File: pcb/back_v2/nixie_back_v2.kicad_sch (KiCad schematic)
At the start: 1 part

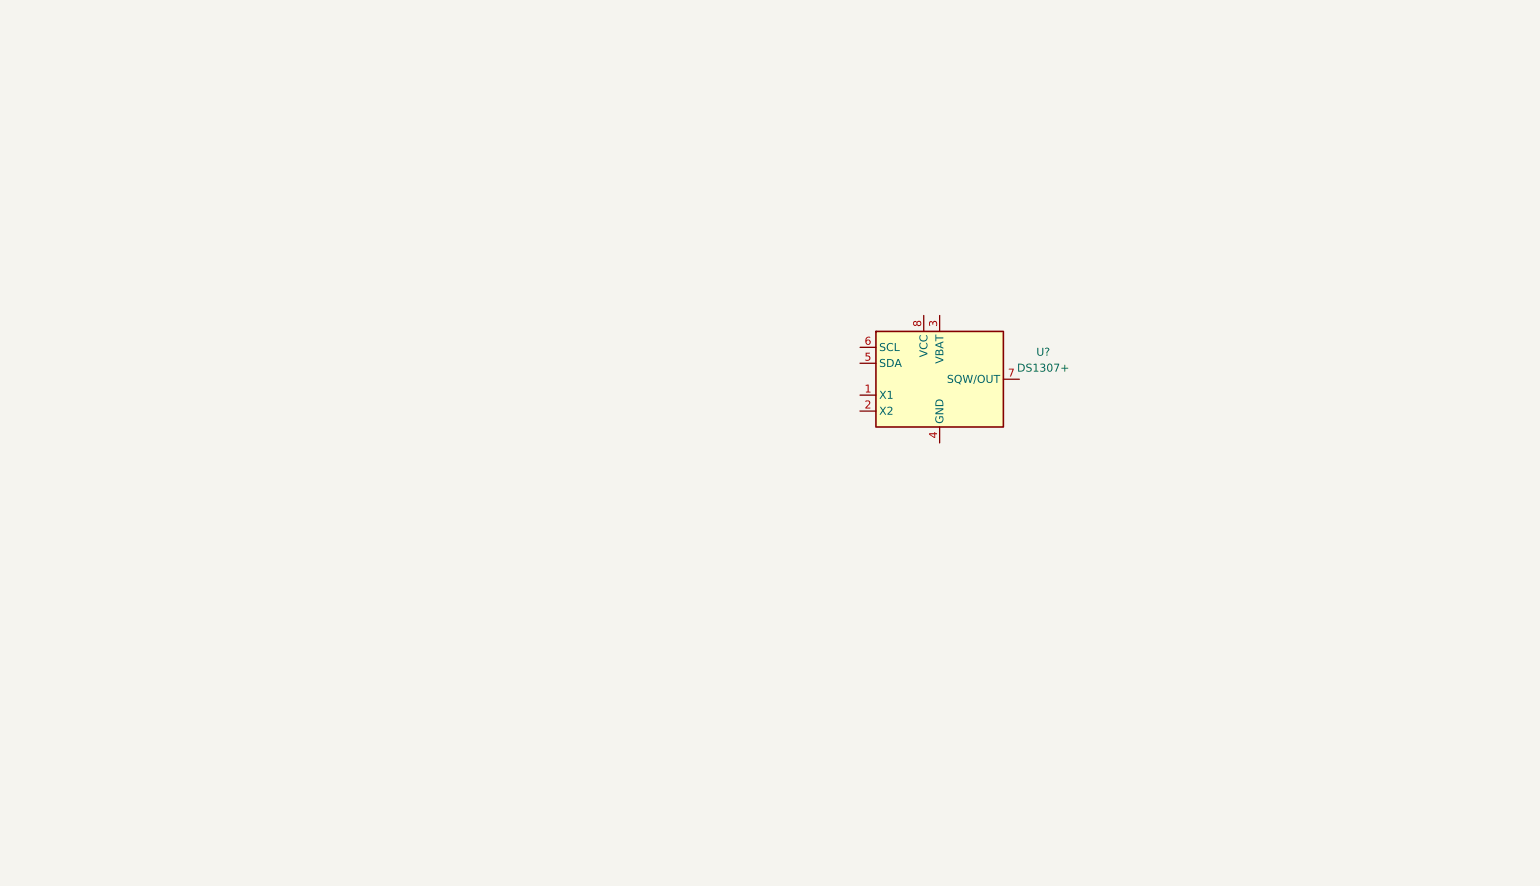
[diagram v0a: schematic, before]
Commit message: Schematic for back PCB v2
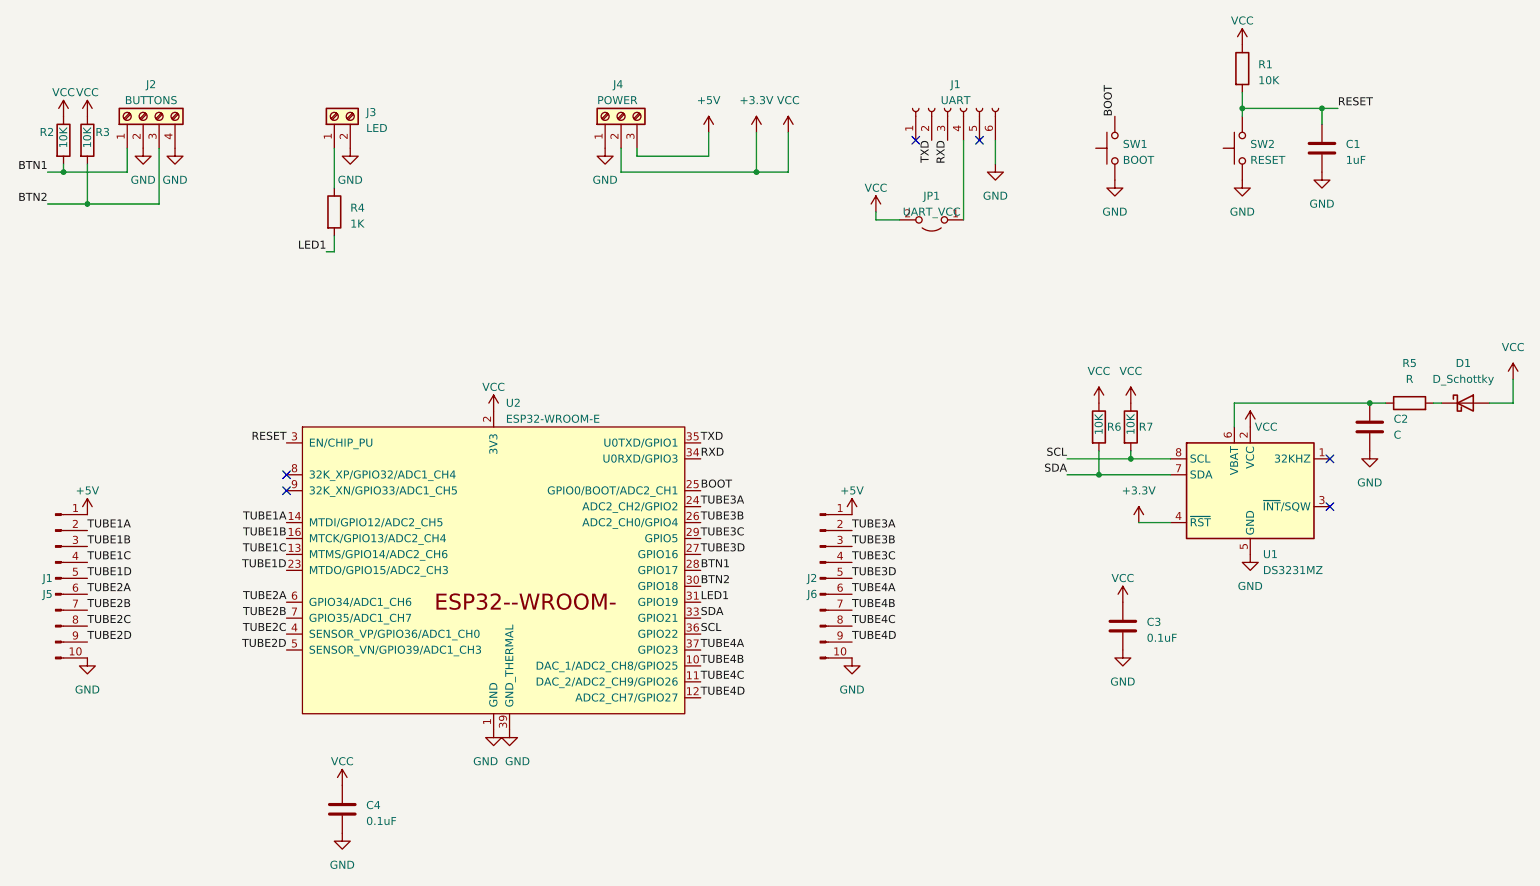
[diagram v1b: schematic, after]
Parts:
- removed U?: DS1307+, Package_DIP:DIP-8_W7.62mm, symbol Timer_RTC:DS1307+
- added C1: 1uF, symbol Device:C
- added C2: C, symbol Device:C
- added C3, C4: 0.1uF, symbol Device:C
- added D1: D_Schottky, symbol Device:D_Schottky
- added J1: UART, symbol Connector:Conn_01x06_Socket
- added J2: BUTTONS, symbol Connector:Screw_Terminal_01x04
- added J3: LED, symbol Connector:Screw_Terminal_01x02
- added J4: POWER, symbol Connector:Screw_Terminal_01x03
- added J5: J1, symbol Connector:Conn_01x10_Pin
- added J6: J2, symbol Connector:Conn_01x10_Pin
- added JP1: UART_VCC, symbol Jumper:Jumper_2_Open
- added R1, R2, R3, R6, R7: 10K, symbol Device:R
- added R4: 1K, symbol Device:R
- added R5: R, symbol Device:R
- added SW1: BOOT, symbol Switch:SW_Push
- added SW2: RESET, symbol Switch:SW_Push
- added U1: DS3231MZ, Package_SO:SOIC-8_3.9x4.9mm_P1.27mm, symbol Timer_RTC:DS3231MZ
- added U2: ESP32-WROOM-E, Espressif:ESP32-WROOM-32E, symbol Espressif:ESP32-WROOM-E
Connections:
- new net: J3.1 (Pin_1), R4.1
- new net: D1.1 (K), R5.2
- new net: J1.4 (Pin_4), JP1.1 (A)
- new net: C2.2, R5.1, U1.6 (VBAT)
- new net +3.3V: C3.1, C4.1, D1.2 (A), J4.2 (Pin_2), JP1.2 (B), R1.1, R2.1, R3.1, R6.1, R7.1, U1.2 (VCC), U1.4 (~{RST}), U2.2 (3V3)
- new net +5V: J4.3 (Pin_3), J5.1 (Pin_1), J6.1 (Pin_1)
- new net BOOT: SW1.2, U2.25 (GPIO0/BOOT/ADC2_CH1)
- new net BTN1: J2.1 (Pin_1), R2.2, U2.28 (GPIO17)
- new net BTN2: J2.3 (Pin_3), R3.2, U2.30 (GPIO18)
- new net GND: C1.2, C2.1, C3.2, C4.2, J1.6 (Pin_6), J2.2 (Pin_2), J2.4 (Pin_4), J3.2 (Pin_2), J4.1 (Pin_1), J5.10 (Pin_10), J6.10 (Pin_10), SW1.1, SW2.1, U1.5 (GND), U2.1 (GND), U2.15 (GND), U2.38 (GND), U2.39 (GND_THERMAL)
- new net LED1: R4.2, U2.31 (GPIO19)
- new net RESET: C1.1, R1.2, SW2.2, U2.3 (EN/CHIP_PU)
- new net RXD: J1.3 (Pin_3), U2.34 (U0RXD/GPIO3)
- new net SCL: R7.2, U1.8 (SCL), U2.36 (GPIO22)
- new net SDA: R6.2, U1.7 (SDA), U2.33 (GPIO21)
- new net TUBE1A: J5.2 (Pin_2), U2.14 (MTDI/GPIO12/ADC2_CH5)
- new net TUBE1B: J5.3 (Pin_3), U2.16 (MTCK/GPIO13/ADC2_CH4)
- new net TUBE1C: J5.4 (Pin_4), U2.13 (MTMS/GPIO14/ADC2_CH6)
- new net TUBE1D: J5.5 (Pin_5), U2.23 (MTDO/GPIO15/ADC2_CH3)
- new net TUBE2A: J5.6 (Pin_6), U2.6 (GPIO34/ADC1_CH6)
- new net TUBE2B: J5.7 (Pin_7), U2.7 (GPIO35/ADC1_CH7)
- new net TUBE2C: J5.8 (Pin_8), U2.4 (SENSOR_VP/GPIO36/ADC1_CH0)
- new net TUBE2D: J5.9 (Pin_9), U2.5 (SENSOR_VN/GPIO39/ADC1_CH3)
- new net TUBE3A: J6.2 (Pin_2), U2.24 (ADC2_CH2/GPIO2)
- new net TUBE3B: J6.3 (Pin_3), U2.26 (ADC2_CH0/GPIO4)
- new net TUBE3C: J6.4 (Pin_4), U2.29 (GPIO5)
- new net TUBE3D: J6.5 (Pin_5), U2.27 (GPIO16)
- new net TUBE4A: J6.6 (Pin_6), U2.37 (GPIO23)
- new net TUBE4B: J6.7 (Pin_7), U2.10 (DAC_1/ADC2_CH8/GPIO25)
- new net TUBE4C: J6.8 (Pin_8), U2.11 (DAC_2/ADC2_CH9/GPIO26)
- new net TUBE4D: J6.9 (Pin_9), U2.12 (ADC2_CH7/GPIO27)
- new net TXD: J1.2 (Pin_2), U2.35 (U0TXD/GPIO1)
- no-connect marks 0 -> 6

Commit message: Lay out the new back panel pcb
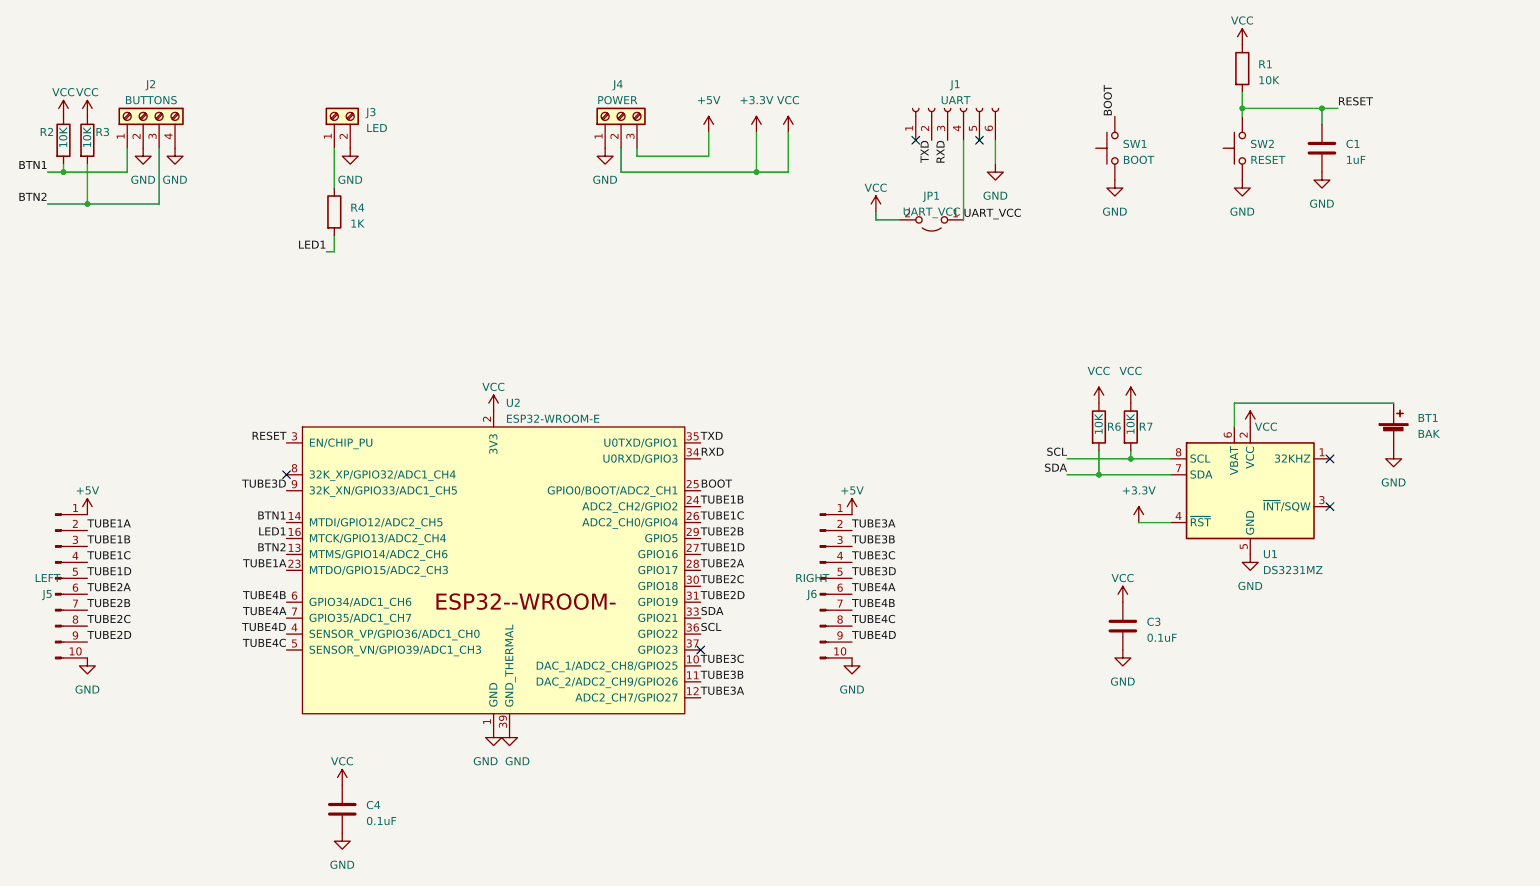
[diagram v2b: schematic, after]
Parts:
- removed C2: C, symbol Device:C
- removed D1: D_Schottky, symbol Device:D_Schottky
- removed R5: R, symbol Device:R
- added BT1: BAK, Battery:BatteryHolder_Keystone_103_1x20mm, symbol Device:Battery_Cell
- C1, C3, C4: footprint (none) -> Capacitor_SMD:C_1206_3216Metric_Pad1.33x1.80mm_HandSolder
- J1: footprint (none) -> Connector_PinHeader_2.54mm:PinHeader_1x06_P2.54mm_Vertical
- J2: footprint (none) -> TerminalBlock:TerminalBlock_Altech_AK300-4_P5.00mm
- J3: footprint (none) -> TerminalBlock:TerminalBlock_Altech_AK300-2_P5.00mm
- J4: footprint (none) -> TerminalBlock:TerminalBlock_Altech_AK300-3_P5.00mm
- J5: value J1 -> LEFT; footprint (none) -> Connector_PinSocket_2.54mm:PinSocket_1x10_P2.54mm_Vertical
- J6: value J2 -> RIGHT; footprint (none) -> Connector_PinSocket_2.54mm:PinSocket_1x10_P2.54mm_Vertical
- JP1: footprint (none) -> Connector_PinHeader_2.54mm:PinHeader_1x02_P2.54mm_Vertical
- R1, R2, R3, R4, R6, R7: footprint (none) -> Resistor_SMD:R_1206_3216Metric_Pad1.30x1.75mm_HandSolder
- SW1, SW2: footprint (none) -> Button_Switch_SMD:SW_Push_1P1T_XKB_TS-1187A
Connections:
- net BTN1: now also U2.14 (MTDI/GPIO12/ADC2_CH5); no longer U2.28 (GPIO17)
- net BTN2: now also U2.13 (MTMS/GPIO14/ADC2_CH6); no longer U2.30 (GPIO18)
- net GND: now also BT1.2 (-)
- net LED1: now also U2.16 (MTCK/GPIO13/ADC2_CH4); no longer U2.31 (GPIO19)
- net TUBE1A: now also U2.23 (MTDO/GPIO15/ADC2_CH3); no longer U2.14 (MTDI/GPIO12/ADC2_CH5)
- net TUBE1B: now also U2.24 (ADC2_CH2/GPIO2); no longer U2.16 (MTCK/GPIO13/ADC2_CH4)
- net TUBE1C: now also U2.26 (ADC2_CH0/GPIO4); no longer U2.13 (MTMS/GPIO14/ADC2_CH6)
- net TUBE1D: now also U2.27 (GPIO16); no longer U2.23 (MTDO/GPIO15/ADC2_CH3)
- net TUBE2A: now also U2.28 (GPIO17); no longer U2.6 (GPIO34/ADC1_CH6)
- net TUBE2B: now also U2.29 (GPIO5); no longer U2.7 (GPIO35/ADC1_CH7)
- net TUBE2C: now also U2.30 (GPIO18); no longer U2.4 (SENSOR_VP/GPIO36/ADC1_CH0)
- net TUBE2D: now also U2.31 (GPIO19); no longer U2.5 (SENSOR_VN/GPIO39/ADC1_CH3)
- net TUBE3A: now also U2.12 (ADC2_CH7/GPIO27); no longer U2.24 (ADC2_CH2/GPIO2)
- net TUBE3B: now also U2.11 (DAC_2/ADC2_CH9/GPIO26); no longer U2.26 (ADC2_CH0/GPIO4)
- net TUBE3C: now also U2.10 (DAC_1/ADC2_CH8/GPIO25); no longer U2.29 (GPIO5)
- net TUBE3D: now also U2.9 (32K_XN/GPIO33/ADC1_CH5); no longer U2.27 (GPIO16)
- net TUBE4A: now also U2.7 (GPIO35/ADC1_CH7); no longer U2.37 (GPIO23)
- net TUBE4B: now also U2.6 (GPIO34/ADC1_CH6); no longer U2.10 (DAC_1/ADC2_CH8/GPIO25)
- net TUBE4C: now also U2.5 (SENSOR_VN/GPIO39/ADC1_CH3); no longer U2.11 (DAC_2/ADC2_CH9/GPIO26)
- net TUBE4D: now also U2.4 (SENSOR_VP/GPIO36/ADC1_CH0); no longer U2.12 (ADC2_CH7/GPIO27)
- net UART_VCC: now reaches J1.4 (Pin_4), JP1.1 (A)
- net at U1.6 (VBAT): now also BT1.1 (+)
